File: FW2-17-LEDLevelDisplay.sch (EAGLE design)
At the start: 60 parts, among them Q1 BC557, Q10 BC547, Q11 BC547, Q2 BC547, Q3 BC547, Q4 BC547, Q5 BC547, Q6 BC547, Q7 BC547, Q8 BC547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

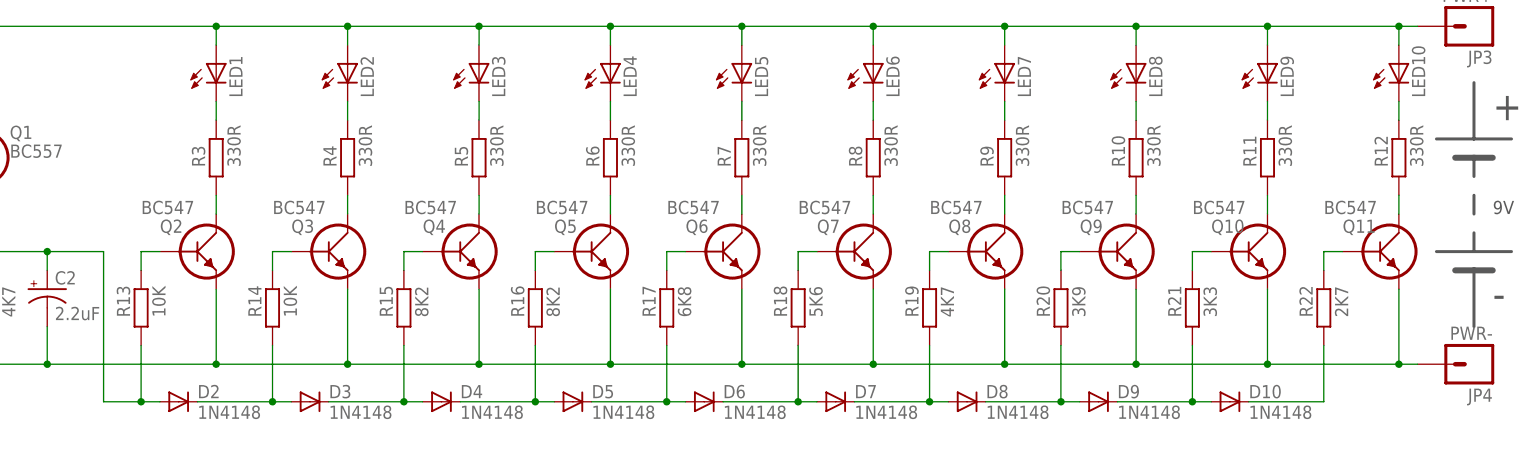
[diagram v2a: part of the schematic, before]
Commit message: Increased pad size; improved silkscreen
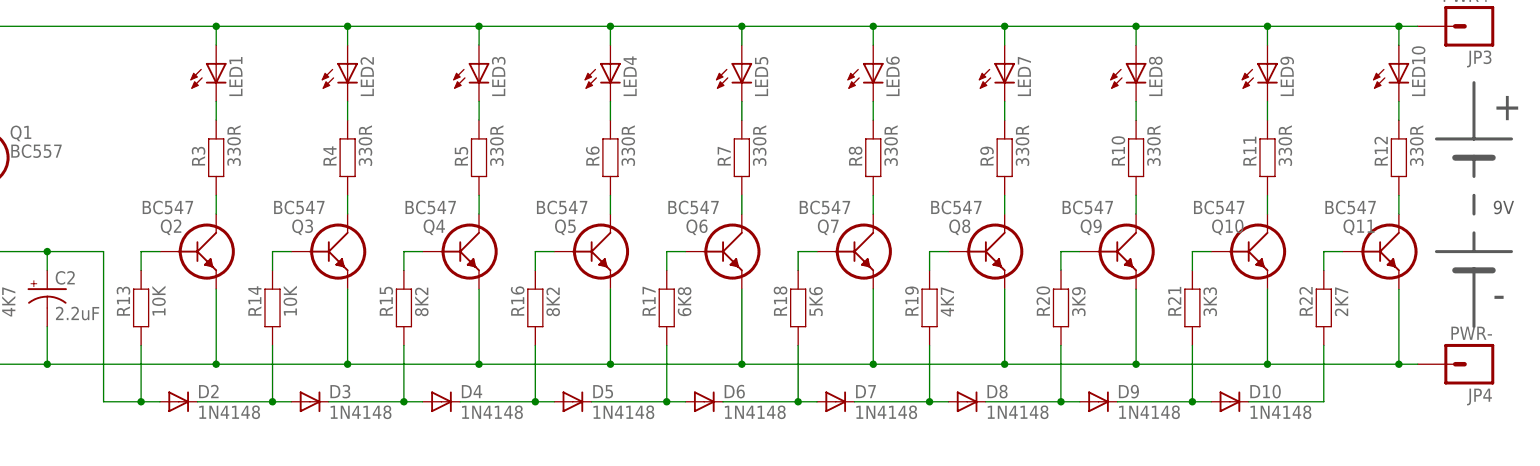
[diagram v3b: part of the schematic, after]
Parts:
- D1, D10, D2, D3, D4, D5, D6, D7, D8, D9: device freetronics-master-v1.1:DIODE1N914 -> freetronics-master-v1.1:DIODE1N914L
- LED1, LED10, LED2, LED3, LED4, LED5, LED6, LED7, LED8, LED9: device freetronics-master-v1.1:LED5MM -> freetronics-master-v1.1:LED5MML
- R1, R2: device freetronics:FREETRONICS_RESISTORPTH2 -> freetronics:FREETRONICS_RESISTORPTH3
- R10, R11, R12, R13, R14, R15, R16, R17, R18, R19, R20, R21, R22, R3, R4, R5, R6, R7, R8, R9: device resistor:R-EU_0309/V -> freetronics-jon:RESISTORVERT3
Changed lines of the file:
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@@
 <parts>
 <part name="Q2" library="freetronics-master-v1.1" deviceset="BC547" device=""/>
-<part name="R13" library="resistor" deviceset="R-EU_" device="0309/V" value="10K"/>
-<part name="R3" library="resistor" deviceset="R-EU_" device="0309/V" value="330R"/>
-<part name="LED1" library="freetronics-master-v1.1" deviceset="LED" device="5MM"/>
+<part name="R13" library="freetronics-jon" deviceset="RESISTOR" device="VERT3" value="10K"/>
+<part name="R3" library="freetronics-jon" deviceset="RESISTOR" device="VERT3" value="330R"/>
+<part name="LED1" library="freetronics-master-v1.1" deviceset="LED" device="5MML"/>
 <part name="Q3" library="freetronics-master-v1.1" deviceset="BC547" device=""/>
-<part name="R14" library="resistor" deviceset="R-EU_" device="0309/V" value="10K"/>
-<part name="R4" library="resistor" deviceset="R-EU_" device="0309/V" value="330R"/>
-<part name="LED2" library="freetronics-master-v1.1" deviceset="LED" device="5MM"/>
-<part name="D2" library="freetronics-master-v1.1" deviceset="DIODE" device="1N914" value="1N4148"/>
-<part name="D3" library="freetronics-master-v1.1" deviceset="DIODE" device="1N914" value="1N4148"/>
-<part name="D4" library="freetronics-master-v1.1" deviceset="DIODE" device="1N914" value="1N4148"/>
-<part name="D5" library="freetronics-master-v1.1" deviceset="DIODE" device="1N914" value="1N4148"/>
-<part name="D6" library="freetronics-master-v1.1" deviceset="DIODE" device="1N914" value="1N4148"/>
+<part name="R14" library="freetronics-jon" deviceset="RESISTOR" device="VERT3" value="10K"/>
+<part name="R4" library="freetronics-jon" deviceset="RESISTOR" device="VERT3" value="330R"/>
+<part name="LED2" library="freetronics-master-v1.1" deviceset="LED" device="5MML"/>
+<part name="D2" library="freetronics-master-v1.1" deviceset="DIODE" device="1N914L" value="1N4148"/>
+<part name="D3" library="freetronics-master-v1.1" deviceset="DIODE" device="1N914L" value="1N4148"/>
+<part name="D4" library="freetronics-master-v1.1" deviceset="DIODE" device="1N914L" value="1N4148"/>
+<part name="D5" library="freetronics-master-v1.1" deviceset="DIODE" device="1N914L" value="1N4148"/>
+<part name="D6" library="freetronics-master-v1.1" deviceset="DIODE" device="1N914L" value="1N4148"/>
 <part name="Q4" library="freetronics-master-v1.1" deviceset="BC547" device=""/>
 <part name="Q5" library="freetronics-master-v1.1" deviceset="BC547" device=""/>
 <part name="Q6" library="freetronics-master-v1.1" deviceset="BC547" device=""/>
-<part name="R5" library="resistor" deviceset="R-EU_" device="0309/V" value="330R"/>
-<part name="R6" library="resistor" deviceset="R-EU_" device="0309/V" value="330R"/>
-<part name="R7" library="resistor" deviceset="R-EU_" device="0309/V" value="330R"/>
-<part name="LED3" library="freetronics-master-v1.1" deviceset="LED" device="5MM"/>
-<part name="LED4" library="freetronics-master-v1.1" deviceset="LED" device="5MM"/>
-<part name="LED5" library="freetronics-master-v1.1" deviceset="LED" device="5MM"/>
-<part name="R15" library="resistor" deviceset="R-EU_" device="0309/V" value="8K2"/>
-<part name="R16" library="resistor" deviceset="R-EU_" device="0309/V" value="8K2"/>
-<part name="R17" library="resistor" deviceset="R-EU_" device="0309/V" value="6K8"/>
+<part name="R5" library="freetronics-jon" deviceset="RESISTOR" device="VERT3" value="330R"/>
+<part name="R6" library="freetronics-jon" deviceset="RESISTOR" device="VERT3" value="330R"/>
+<part name="R7" library="freetronics-jon" deviceset="RESISTOR" device="VERT3" value="330R"/>
+<part name="LED3" library="freetronics-master-v1.1" deviceset="LED" device="5MML"/>
+<part name="LED4" library="freetronics-master-v1.1" deviceset="LED" device="5MML"/>
+<part name="LED5" library="freetronics-master-v1.1" deviceset="LED" device="5MML"/>
+<part name="R15" library="freetronics-jon" deviceset="RESISTOR" device="VERT3" value="8K2"/>
+<part name="R16" library="freetronics-jon" deviceset="RESISTOR" device="VERT3" value="8K2"/>
+<part name="R17" library="freetronics-jon" deviceset="RESISTOR" device="VERT3" value="6K8"/>
 <part name="Q7" library="freetronics-master-v1.1" deviceset="BC547" device=""/>
 <part name="Q8" library="freetronics-master-v1.1" deviceset="BC547" device=""/>
 <part name="Q9" library="freetronics-master-v1.1" deviceset="BC547" device=""/>
 <part name="Q10" library="freetronics-master-v1.1" deviceset="BC547" device=""/>
-<part name="R18" library="resistor" deviceset="R-EU_" device="0309/V" value="5K6"/>
-<part name="R19" library="resistor" deviceset="R-EU_" device="0309/V" value="4K7"/>
-<part name="R20" library="resistor" deviceset="R-EU_" device="0309/V" value="3K9"/>
-<part name="R21" library="resistor" deviceset="R-EU_" device="0309/V" value="3K3"/>
-<part name="R8" library="resistor" deviceset="R-EU_" device="0309/V" value="330R"/>
-<part name="R9" library="resistor" deviceset="R-EU_" device="0309/V" value="330R"/>
-<part name="R10" library="resistor" deviceset="R-EU_" device="0309/V" value="330R"/>
-<part name="R11" library="resistor" deviceset="R-EU_" device="0309/V" value="330R"/>
-<part name="LED6" library="freetronics-master-v1.1" deviceset="LED" device="5MM"/>
-<part name="LED7" library="freetronics-master-v1.1" deviceset="LED" device="5MM"/>
-<part name="LED8" library="freetronics-master-v1.1" deviceset="LED" device="5MM"/>
-<part name="LED9" library="freetronics-master-v1.1" deviceset="LED" device="5MM"/>
-<part name="D7" library="freetronics-master-v1.1" deviceset="DIODE" device="1N914" value="1N4148"/>
-<part name="D8" library="freetronics-master-v1.1" deviceset="DIODE" device="1N914" value="1N4148"/>
-<part name="D9" library="freetronics-master-v1.1" deviceset="DIODE" device="1N914" value="1N4148"/>
+<part name="R18" library="freetronics-jon" deviceset="RESISTOR" device="VERT3" value="5K6"/>
+<part name="R19" library="freetronics-jon" deviceset="RESISTOR" device="VERT3" value="4K7"/>
+<part name="R20" library="freetronics-jon" deviceset="RESISTOR" device="VERT3" value="3K9"/>
+<part name="R21" library="freetronics-jon" deviceset="RESISTOR" device="VERT3" value="3K3"/>
+<part name="R8" library="freetronics-jon" deviceset="RESISTOR" device="VERT3" value="330R"/>
+<part name="R9" library="freetronics-jon" deviceset="RESISTOR" device="VERT3" value="330R"/>
+<part name="R10" library="freetronics-jon" deviceset="RESISTOR" device="VERT3" value="330R"/>
+<part name="R11" library="freetronics-jon" deviceset="RESISTOR" device="VERT3" value="330R"/>
+<part name="LED6" library="freetronics-master-v1.1" deviceset="LED" device="5MML"/>
+<part name="LED7" library="freetronics-master-v1.1" deviceset="LED" device="5MML"/>
+<part name="LED8" library="freetronics-master-v1.1" deviceset="LED" device="5MML"/>
+<part name="LED9" library="freetronics-master-v1.1" deviceset="LED" device="5MML"/>
+<part name="D7" library="freetronics-master-v1.1" deviceset="DIODE" device="1N914L" value="1N4148"/>
+<part name="D8" library="freetronics-master-v1.1" deviceset="DIODE" device="1N914L" value="1N4148"/>
+<part name="D9" library="freetronics-master-v1.1" deviceset="DIODE" device="1N914L" value="1N4148"/>
 <part name="JP1" library="freetronics-master-v1.1" deviceset="M01" device="PTH" value="IN+"/>
 <part name="JP2" library="freetronics-master-v1.1" deviceset="M01" device="PTH" value="IN-"/>
@@
 <part name="C2" library="SparkFun" deviceset="CAP_POL" device="PTH1" value="2.2uF"/>
 <part name="C1" library="SparkFun" deviceset="CAP_POL" device="PTH1" value="2.2uF"/>
-<part name="R2" library="freetronics" deviceset="FREETRONICS_RESISTOR" device="PTH2" value="4K7"/>
+<part name="R2" library="freetronics" deviceset="FREETRONICS_RESISTOR" device="PTH3" value="4K7"/>
 <part name="VR1" library="adafruit" deviceset="TRIM" device="" value="100K"/>
-<part name="LED10" library="freetronics-master-v1.1" deviceset="LED" device="5MM"/>
-<part name="R12" library="resistor" deviceset="R-EU_" device="0309/V" value="330R"/>
+<part name="LED10" library="freetronics-master-v1.1" deviceset="LED" device="5MML"/>
+<part name="R12" library="freetronics-jon" deviceset="RESISTOR" device="VERT3" value="330R"/>
 <part name="Q11" library="freetronics-master-v1.1" deviceset="BC547" device=""/>
-<part name="R22" library="resistor" deviceset="R-EU_" device="0309/V" value="2K7"/>
-<part name="D10" library="freetronics-master-v1.1" deviceset="DIODE" device="1N914" value="1N4148"/>
-<part name="D1" library="freetronics-master-v1.1" deviceset="DIODE" device="1N914" value="1N4148"/>
-<part name="R1" library="freetronics" deviceset="FREETRONICS_RESISTOR" device="PTH2" value="470R"/>
+<part name="R22" library="freetronics-jon" deviceset="RESISTOR" device="VERT3" value="2K7"/>
+<part name="D10" library="freetronics-master-v1.1" deviceset="DIODE" device="1N914L" value="1N4148"/>
+<part name="D1" library="freetronics-master-v1.1" deviceset="DIODE" device="1N914L" value="1N4148"/>
+<part name="R1" library="freetronics" deviceset="FREETRONICS_RESISTOR" device="PTH3" value="470R"/>
 <part name="Q1" library="freetronics-master-v1.1" deviceset="BC557" device=""/>
 </parts>
@@
 </sheet>
 </sheets>
+<errors>
+</errors>
 </schematic>
 </drawing>
